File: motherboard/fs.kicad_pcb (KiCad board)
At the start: 4 copper layers, 177.8 x 114.3 mm, 247 parts, among them J101 Header, J102 640389-2, J201 BNC, J202 Conn_01x05, J203 BNC, J301 BNC, J302 BNC, J303 BNC, J304 BNC, J305 BNC, J306 BNC, Q101 MJD44H11, Q102 MJD45H11, Q201 2N7002, Q202 2N7002, Q203 2N7002, U101 INA132UA, U102 LM741C, U103 LMH6609, U104 LM317, U105 LM337, U106 LM340-5, U107 MC7905ACD2T, U201 LMH6609, U202 SYPD-1, U203 LM393, U204 AD797AR, U205 LM393, U206 OPA192IDR, U301 LMH6609, U302 LMH6609, U303 LMH6609, U304 LMH6609, U305 LMH6609, U306 LMH6609

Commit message: make FREQ_CTL filter cap an NP0 part
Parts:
- added R231: 100R 0.5W, Resistor_SMD:R_1206_3216Metric, F.Cu at (72.4, 134.1)
- added R319: 100R 0.5W, Resistor_SMD:R_1206_3216Metric, F.Cu at (92.2, 134.1)
- added R320: 100R 0.5W, Resistor_SMD:R_1206_3216Metric, F.Cu at (112.5, 134.1)
- added R321: 100R 0.5W, Resistor_SMD:R_1206_3216Metric, F.Cu at (132.7, 134.1)
- added R322: 100R 0.5W, Resistor_SMD:R_1206_3216Metric, F.Cu at (173.5, 134.2)
- added R323: 100R 0.5W, Resistor_SMD:R_1206_3216Metric, F.Cu at (193.9, 134.2)
- added R326: 100R 0.5W, Resistor_SMD:R_1206_3216Metric, F.Cu at (153.3, 134.2)
- C102: value 10μF -> 0.1μF C0G; footprint Capacitor_SMD:C_0805_2012Metric -> Capacitor_SMD:C_1206_3216Metric
- R209: value 49.9R 1W -> 49.9R; footprint Resistor_SMD:R_2512_6332Metric -> Resistor_SMD:R_0603_1608Metric
- R223, R307, R308, R309, R316, R317, R318: value 49.9R 1W -> 100R 0.5W; footprint Resistor_SMD:R_2512_6332Metric -> Resistor_SMD:R_1206_3216Metric
- moved R102 4.00 mm to (122.0, 69.1), turned to -90 degrees
- moved R209 2.07 mm to (54.6, 113.0)
- moved R223 1.98 mm to (74.7, 134.1)
- moved R318 1.81 mm to (196.2, 134.3)
- moved R316 1.80 mm to (155.6, 134.2)
- moved R317 1.73 mm to (175.8, 134.2)
- moved R307 1.63 mm to (94.5, 134.1)
- moved R308 1.62 mm to (114.8, 134.1)
- moved R309 1.61 mm to (135.1, 134.1)
- moved R224 1.40 mm to (71.1, 129.7)
- moved C102 1.32 mm to (118.7, 69.5)
- moved D303 0.76 mm to (130.6, 135.8)
- moved D302 0.73 mm to (110.3, 135.8)
- moved D305 0.51 mm to (171.4, 135.8)
- moved D301 0.48 mm to (90.1, 135.8)
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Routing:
- net Net-(R314-Pad1): track 6.99 -> 12.3 mm
- net Net-(R315-Pad1): track 6.99 -> 12.2 mm
- net Net-(R313-Pad1): track 6.99 -> 12.2 mm
- net Net-(R306-Pad1): track 6.99 -> 12.2 mm
- net Net-(R304-Pad1): track 6.99 -> 12.2 mm
- net Net-(R305-Pad1): track 6.99 -> 12.1 mm
- net Net-(R204-Pad1): track 6.69 -> 10.9 mm
- net /Outputs/OUT3: track 13.9 -> 18.1 mm
- net /Outputs/OUT2: track 13.9 -> 18.1 mm
- net Net-(R221-Pad1): track 9.54 -> 13.3 mm
- net /Outputs/OUT5: track 14.0 -> 16.9 mm
- net /Outputs/OUT6: track 14.1 -> 16.7 mm
- net Net-(D203-CATHODE): track 8.01 -> 10.3 mm
- net /Outputs/OUT4: track 13.9 -> 15.4 mm
- net Net-(Q202-S): track 28.3 -> 29.7 mm
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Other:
- board text added: "B.Cu"
- board text added: "B.Mask"
- board text added: "B.Paste"
- board text added: "B.Silkscreen"
- board text added: "F.Cu"
- board text added: "F.Mask"
- board text added: "F.Paste"
- board text added: "F.Silkscreen"
- board text added: "In1.Cu"
- board text added: "In2.Cu"

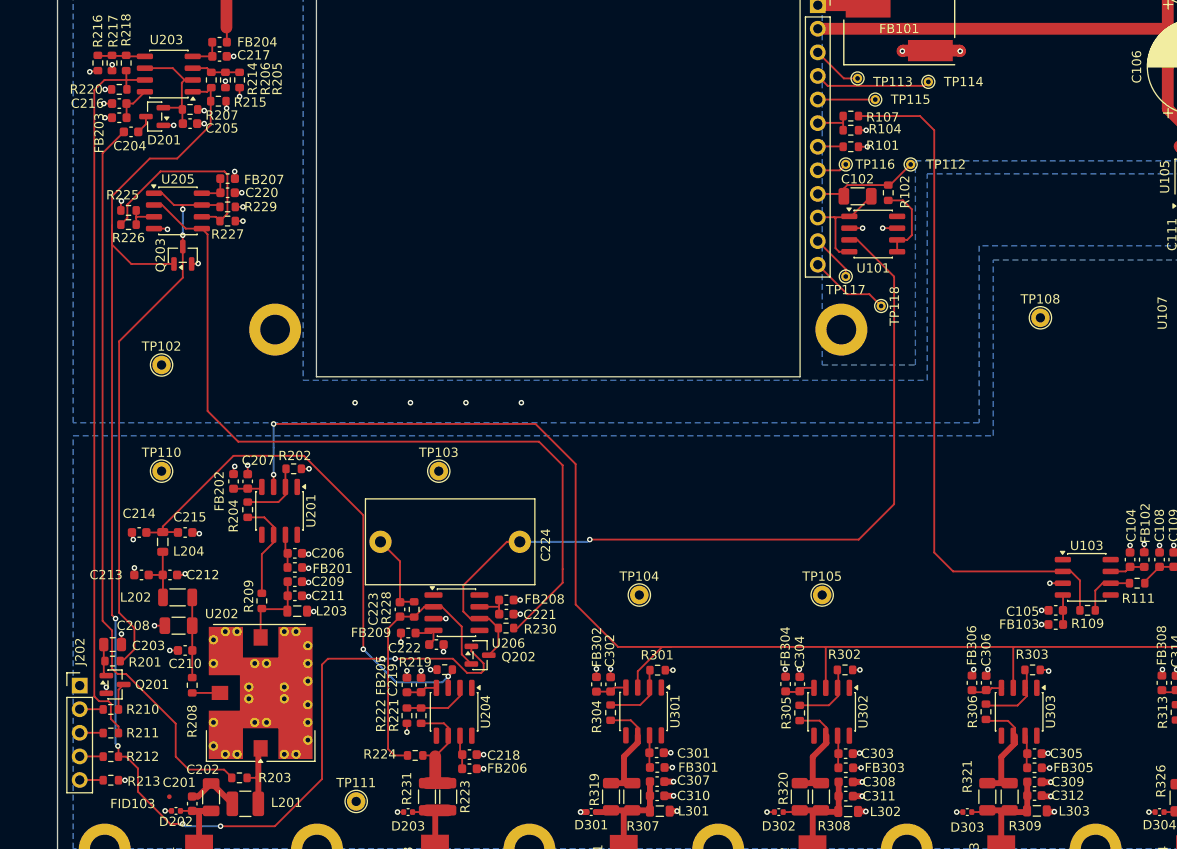
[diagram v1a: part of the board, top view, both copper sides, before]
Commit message: replace mosfet with analog switch
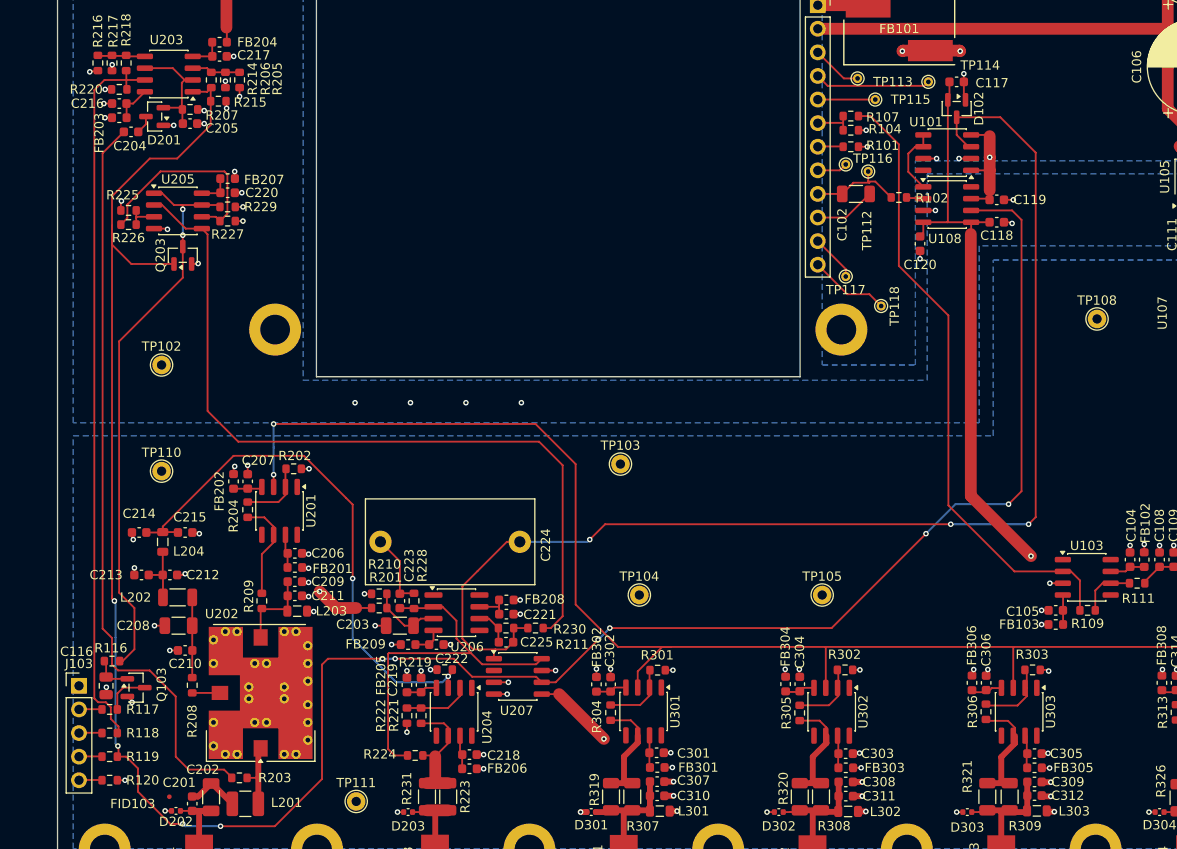
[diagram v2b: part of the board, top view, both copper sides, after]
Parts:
- removed J202: Conn_01x05, Connector_PinHeader_2.54mm:PinHeader_1x05_P2.54mm_Vertical
- removed Q201, Q202: 2N7002, Package_TO_SOT_SMD:SOT-23
- removed R212: 4.99K, Resistor_SMD:R_0603_1608Metric
- removed R213: 1.00K, Resistor_SMD:R_0603_1608Metric
- added C116: 10μF, Capacitor_SMD:C_0805_2012Metric, F.Cu at (37.8, 122.2)
- added C117: 0.1μF, Capacitor_SMD:C_0603_1608Metric, F.Cu at (129.4, 57.1)
- added C118: 0.1μF, Capacitor_SMD:C_0603_1608Metric, F.Cu at (133.7, 72.3)
- added C119: 0.1μF, Capacitor_SMD:C_0603_1608Metric, F.Cu at (133.7, 69.8)
- added C120: 0.1μF, Capacitor_SMD:C_0603_1608Metric, F.Cu at (125.5, 74.6)
- added C225: 1nF NP0, Capacitor_SMD:C_0603_1608Metric, F.Cu at (80.9, 117.5)
- added D102: MMBD352, Package_TO_SOT_SMD:SOT-23, F.Cu at (129.4, 60.0)
- added J103: Conn_01x05, Connector_PinHeader_2.54mm:PinHeader_1x05_P2.54mm_Vertical, F.Cu at (34.9, 122.2)
- added Q103: 2N7002, Package_TO_SOT_SMD:SOT-23, F.Cu at (41.1, 122.4)
- added R116: 10.0K, Resistor_SMD:R_0603_1608Metric, F.Cu at (38.5, 119.5)
- added R117: 1.00K, Resistor_SMD:R_0603_1608Metric, F.Cu at (38.2, 124.7)
- added R118: 4.99K, Resistor_SMD:R_0603_1608Metric, F.Cu at (38.2, 127.3)
- added R119: 4.99K, Resistor_SMD:R_0603_1608Metric, F.Cu at (38.2, 129.8)
- added R120: 1.00K, Resistor_SMD:R_0603_1608Metric, F.Cu at (38.2, 132.3)
- added U108: DG419DY, Package_SO:SO-8_3.9x4.9mm_P1.27mm, F.Cu at (128.4, 70.4)
- added U207: DG419DY, Package_SO:SO-8_3.9x4.9mm_P1.27mm, F.Cu at (82.2, 121.2)
- C203: value 10μF -> 0.1μF C0G; footprint Capacitor_SMD:C_0805_2012Metric -> Capacitor_SMD:C_1206_3216Metric
- D101: value MBRS230LT3G -> MMBD352LT1G
- R210: value 1.00K -> 10.0K
- R211: value 4.99K -> 1.00K
- moved R211 44.0 mm to (80.9, 116.0), turned to 0 degrees
- moved R210 31.5 mm to (67.2, 112.3), turned to 0 degrees
- moved C203 31.0 mm to (69.5, 115.7), turned to 180 degrees
- moved R201 29.3 mm to (67.2, 113.8)
- moved TP103 19.6 mm to (93.2, 98.3)
- moved U101 11.8 mm to (128.4, 64.8), turned to 180 degrees
- moved TP108 6.10 mm to (144.5, 82.7)
- moved TP112 4.64 mm to (119.9, 66.8)
- moved R230 3.17 mm to (84.1, 116.0)
- moved R102 1.25 mm to (123.2, 69.6), turned to 0 degrees
- moved FB209 1.24 mm to (70.4, 117.7)
- moved C223 0.92 mm to (69.5, 113.0)
- moved R228 0.92 mm to (71.0, 113.0)
- moved C102 0.31 mm to (118.6, 69.2)
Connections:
- net /FREQ_CTL renamed /SC10L_FREQ_CTL
- net /Phase Noise/~{SIG_PRESENT} renamed /~{SIG_PRESENT}
- C203 pad 1: Net-(Q201-G) -> Net-(U206-+)
- Q203 pad 3: /Phase Noise/LOCKED -> /LOCKED
- R102 pad 2: Net-(U101-SENSE) -> Net-(R102-Pad2)
- R201 pad 1: /Phase Noise/LOCKED -> Net-(U206-+)
- R201 pad 2: Net-(Q201-G) -> +5V
- R210 pad 1: Net-(Q201-D) -> GND
- R210 pad 2: Net-(J202-Pin_2) -> Net-(U206-+)
- R211 pad 1: /Phase Noise/~{OVLD} -> Net-(C225-Pad2)
- R211 pad 2: Net-(J202-Pin_3) -> /Phase Noise/FREQ_CTL
- R218 pad 2: /Phase Noise/~{OVLD} -> /~{OVLD}
- R220 pad 1: /Phase Noise/~{OVLD} -> /~{OVLD}
- R229 pad 1: /Phase Noise/LOCKED -> /LOCKED
- U203 pad 7: /Phase Noise/~{OVLD} -> /~{OVLD}
- U205 pad 1: /Phase Noise/LOCKED -> /LOCKED
- U205 pad 7: /Phase Noise/LOCKED -> /LOCKED
- U206 pad 3: GND -> Net-(U206-+)
- U206 pad 6: /Phase Noise/FREQ_CTL -> Net-(C225-Pad2)
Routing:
- net /~{SIG_PRESENT}: track 152.7 -> 251.3 mm, vias 6 -> 10
- net /Phase Noise/~{OVLD}: track 78.8 -> 0.00 mm
- net /~{OVLD}: track 0.00 -> 78.7 mm
- net +5V: track 18.6 -> 96.3 mm, vias 14 -> 17
- net /LOCKED: track 0.00 -> 61.2 mm, vias 0 -> 2
- net /Phase Noise/LOCKED: track 61.2 -> 0.00 mm, vias 2 -> 0
- net /Phase Noise/FREQ_CTL: track 91.6 -> 134.2 mm, vias 1 -> 3
- net Net-(U206-–): track 29.7 -> 40.8 mm
- net GND: track 100.8 -> 109.3 mm, vias 109 -> 116
- net -12V: track 256.9 -> 264.8 mm, vias 7 -> 8
- net Net-(U206-+): track 0.00 -> 7.65 mm
- net /10MHZ_DIV: track 74.4 -> 67.4 mm
- net Net-(Q103-D): track 0.00 -> 4.93 mm
- net Net-(C225-Pad2): track 0.00 -> 4.00 mm
- net Net-(Q103-G): track 0.00 -> 3.89 mm
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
